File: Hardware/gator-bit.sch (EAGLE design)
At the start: 77 parts, among them J19 GATOR, J2 GATOR, J20 GATOR, J21 GATOR, J22 GATOR, J25 GATOR, J28 GATOR, J3 GATOR, J32 GATOR, J33 GATOR, J34 GATOR, J35 GATOR, J36 GATOR, J39 GATOR, J4 GATOR, J40 GATOR, U1 TPS63070, U2 micro:bit

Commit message: Updated Brd and Sch files
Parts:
- removed S2: (no value), SparkFun-Switches:SWITCH-SPDT-SMD-AYZ0202
- added C10, C11: 0.1uF, SparkFun-Capacitors:0.1UF-0603-25V-(+80/-20%)
- added C12, C13: 10uF, SparkFun-Capacitors:10UF-POLAR-EIA3216-16V-10%(TANT)
- added J1: GATOR, TAB:GATOR
- added S1: (no value), SparkFun-Switches:SWITCH-DPDT-SMD-AYZ0202
- added U3: 3.3V/150mA, SparkFun-IC-Power:V_REG_MIC52053.3V
- added U4: V_REG_MIC52053.0V, SparkFun-IC-Power:V_REG_MIC52053.0V
- C7: value 10uF -> 33UF; device SparkFun-Capacitors:10UF-0603-6.3V-20% -> SparkFun-Capacitors:33UF20%-6.3V-0805
- R3: value 274K -> 523k; device SparkFun-Resistors:274KOHMOHMS-0603-1/10W-1% -> SparkFun-Resistors:523KOHMOHMS-0603-1/10W-1%
- renumbered LOGO2 to GND
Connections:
- new net 3.0V: C10.1, C13.+, D11.C, D13.C, D15.C, D19.C, D21.C, D23.C, D25.C, U2.3.3V, U4.OUT
- new net 5V: C6.1, C9.1, R1.2, R3.2, S1.5, U1.VOUT, U3.EN, U3.IN, U4.EN, U4.IN
- new net VOUT5.0: J1.P$1, S1.6
- net 3.3V: now also C11.1, C12.+, S1.2, U3.OUT; no longer C6.1, C9.1, D11.C, D13.C, D15.C, D19.C, D21.C, D23.C, D25.C, R1.2, R3.2, S2.P, U1.VOUT, U2.3.3V
- net GND: now also C10.2, C11.2, C12.-, C13.-, U3.GND, U4.GND
- net P0: no longer R14.1
- net PD: now also R14.1
- net VOUT3.3: now also S1.3; no longer S2.S

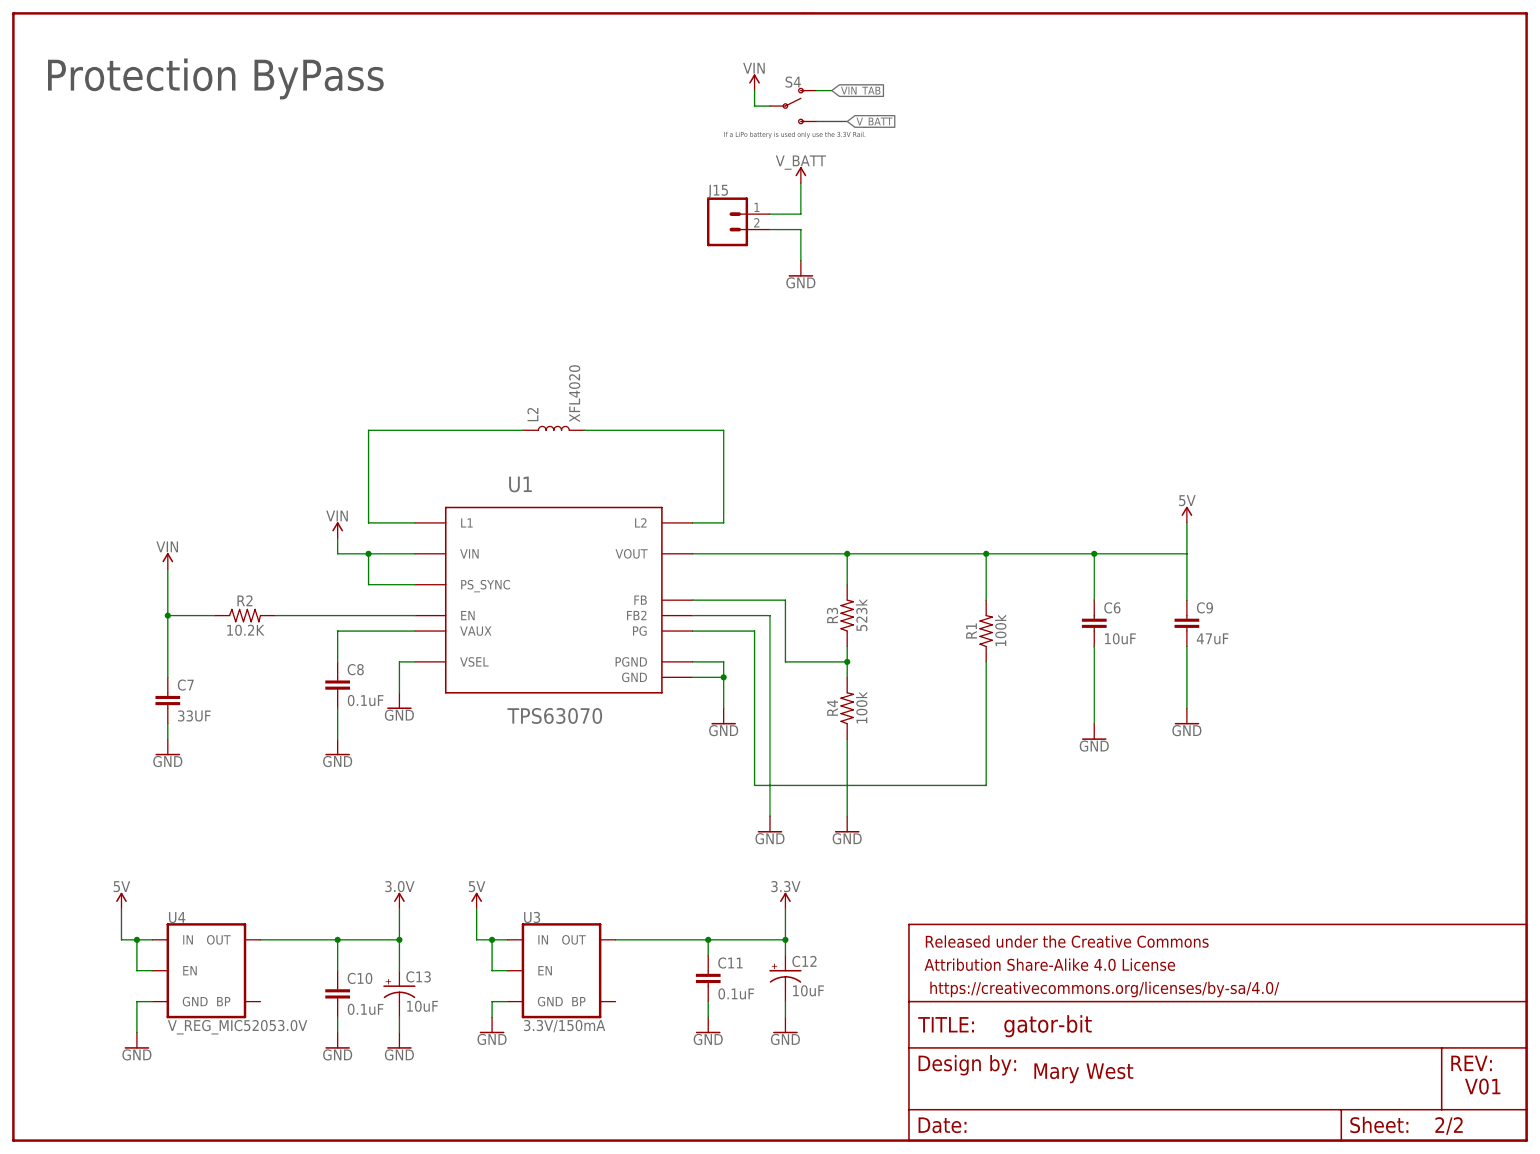
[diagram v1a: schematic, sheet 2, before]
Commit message: added SOT223 package for 3.3V regulated output
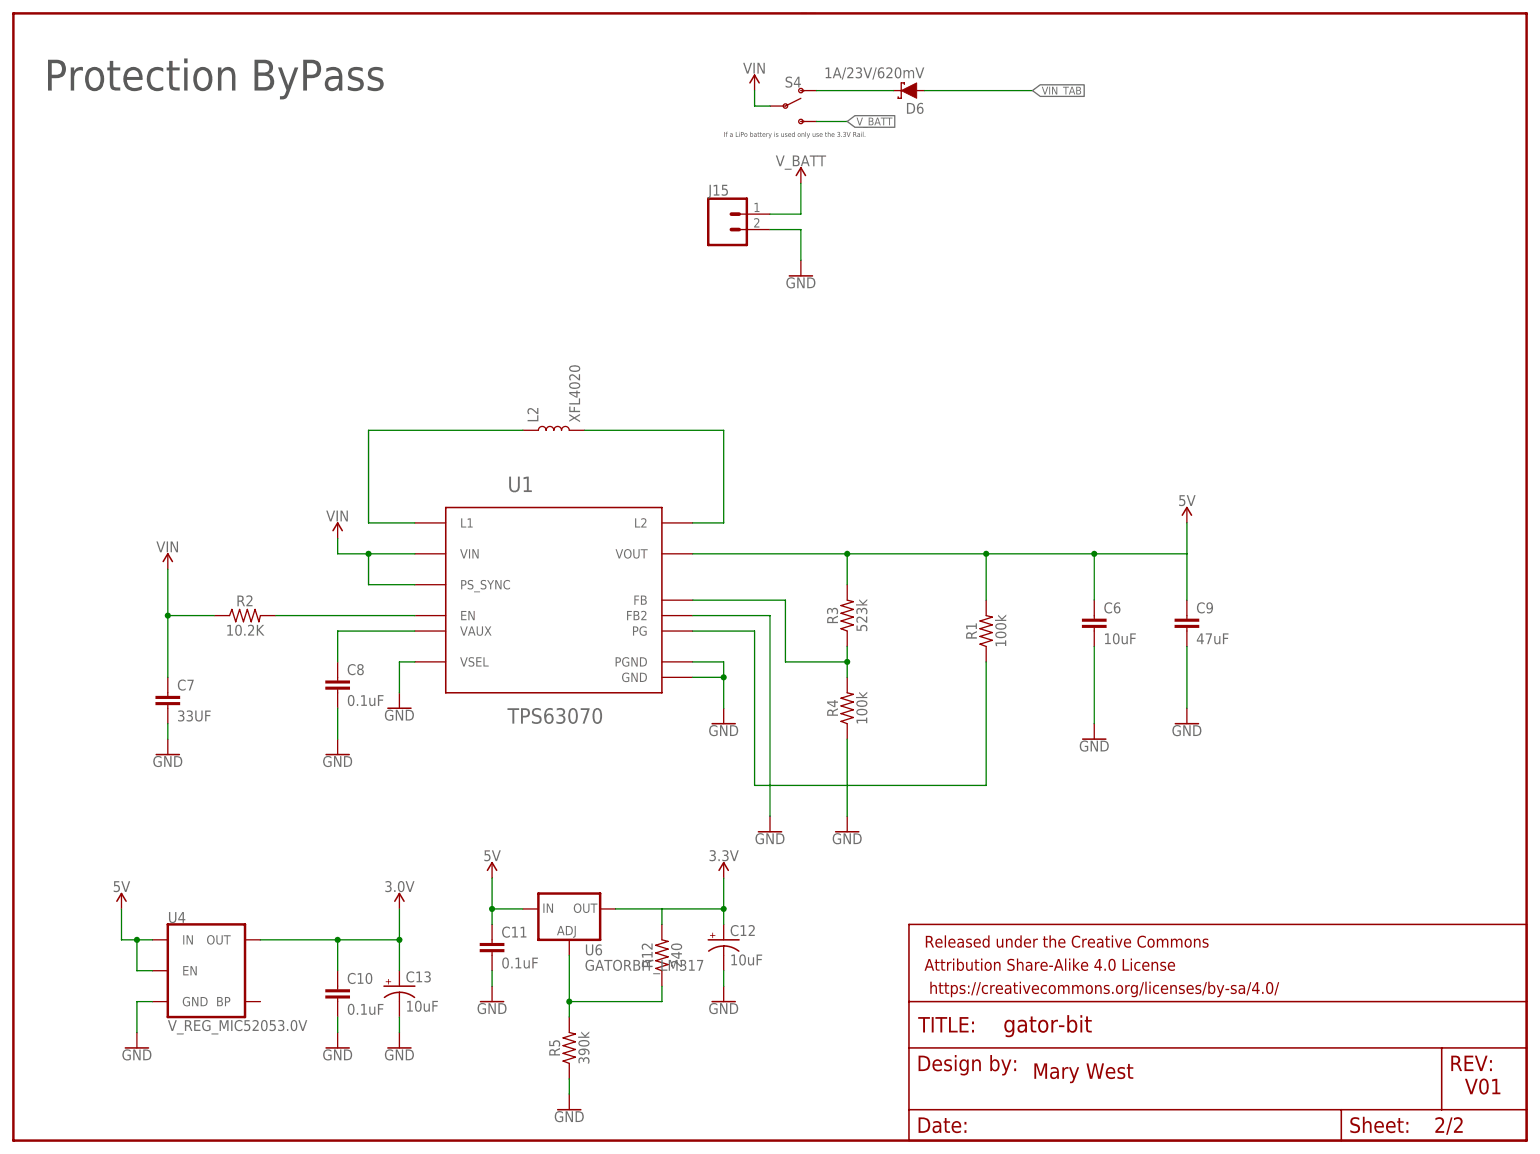
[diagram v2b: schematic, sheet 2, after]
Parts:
- removed U3: 3.3V/150mA, SparkFun-IC-Power:V_REG_MIC52053.3V
- added D6: 1A/23V/620mV, SparkFun-DiscreteSemi:DIODE-SCHOTTKY-BAT20J
- added FD3: FIDUCIAL1X2, SparkFun-Aesthetics:FIDUCIAL1X2
- added LOGO3: SFE_LOGO_NAME_FLAME.3_INCH, SparkFun-Aesthetics:SFE_LOGO_NAME_FLAME.3_INCH
- added R12: 240, SparkFun-Resistors:240OHM-0603-1/10W-1%
- added R5: 390k, SparkFun-Resistors:390KOHM-0603-1/10W-1%
- added U6: GATORBIT_LM317, SparkFun-IC-Power:GATORBIT_LM317
- renumbered GND to LOGO2
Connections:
- new net N$16: R12.1, R5.2, U6.ADJ
- new net N$9: D6.C, S4.O
- net 3.3V: now also R12.2, U6.OUT; no longer C11.1, U3.OUT
- net 5V: now also C11.1, U6.IN; no longer U3.EN, U3.IN
- net GND: now also R5.1; no longer U3.GND
- net VIN_TAB: now also D6.A; no longer S4.O
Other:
- moved on the sheet: C11, C12
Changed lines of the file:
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@@
 <part name="SUPPLY5" library="SparkFun-PowerSymbols" deviceset="3.3V" device=""/>
 <part name="SUPPLY9" library="SparkFun-PowerSymbols" deviceset="3.3V" device=""/>
-<part name="GND" library="SparkFun-Aesthetics" deviceset="OSHW-LOGO" device="L" value="OSHW-LOGOL"/>
 <part name="D11" library="SparkFun-DiscreteSemi" deviceset="DIODE-ZENER" device="-MM3Z3V3T1G" value="3.3V"/>
 <part name="SUPPLY7" library="SparkFun-PowerSymbols" deviceset="3.3V" device="" value="3.0V"/>
@@
 <part name="GND18" library="SparkFun-PowerSymbols" deviceset="GND" device=""/>
 <part name="GND20" library="SparkFun-PowerSymbols" deviceset="GND" device=""/>
-<part name="U3" library="SparkFun-IC-Power" deviceset="V_REG_MIC5205" device="3.3V" value="3.3V/150mA"/>
 <part name="U4" library="SparkFun-IC-Power" deviceset="V_REG_MIC5205" device="3.0V"/>
 <part name="SUPPLY20" library="SparkFun-PowerSymbols" deviceset="5V" device=""/>
@@
 <part name="SUPPLY26" library="SparkFun-PowerSymbols" deviceset="3.3V" device="" value="3.0V"/>
 <part name="SUPPLY27" library="SparkFun-PowerSymbols" deviceset="3.3V" device=""/>
+<part name="D6" library="SparkFun-DiscreteSemi" deviceset="DIODE-SCHOTTKY" device="-BAT20J" value="1A/23V/620mV"/>
+<part name="FD3" library="SparkFun-Aesthetics" deviceset="FIDUCIAL" device="1X2"/>
+<part name="LOGO2" library="SparkFun-Aesthetics" deviceset="OSHW-LOGO" device="L"/>
+<part name="LOGO3" library="SparkFun-Aesthetics" deviceset="SFE_LOGO_NAME_FLAME" device=".3_INCH"/>
+<part name="U6" library="SparkFun-IC-Power" deviceset="GATORBIT_LM317" device=""/>
+<part name="R5" library="SparkFun-Resistors" deviceset="390KOHM" device="-0603-1/10W-1%" value="390k"/>
+<part name="R12" library="SparkFun-Resistors" deviceset="240OHM" device="-0603-1/10W-1%" value="240"/>
 <part name="GND28" library="SparkFun-PowerSymbols" deviceset="GND" device=""/>
 </parts>
@@
 <instance part="SUPPLY5" gate="G$1" x="7.62" y="96.52"/>
 <instance part="SUPPLY9" gate="G$1" x="86.36" y="35.56"/>
-<instance part="GND" gate="G$1" x="167.64" y="45.72"/>
 <instance part="D11" gate="G$1" x="218.44" y="66.04" rot="R90"/>
 <instance part="SUPPLY7" gate="G$1" x="218.44" y="71.12"/>
@@
 <instance part="SUPPLY24" gate="G$1" x="203.2" y="127"/>
 <instance part="SUPPLY25" gate="G$1" x="226.06" y="127"/>
+<instance part="FD3" gate="G$1" x="238.76" y="33.02"/>
+<instance part="LOGO2" gate="G$1" x="167.64" y="45.72"/>
+<instance part="LOGO3" gate="G$1" x="193.04" y="33.02"/>
 </instances>
 <busses>
@@
 <instance part="GND18" gate="1" x="177.8" y="66.04"/>
 <instance part="GND20" gate="1" x="193.04" y="68.58"/>
-<instance part="U3" gate="U1" x="91.44" y="27.94"/>
 <instance part="U4" gate="U1" x="33.02" y="27.94"/>
 <instance part="SUPPLY20" gate="G$1" x="193.04" y="101.6"/>
 <instance part="SUPPLY21" gate="G$1" x="17.78" y="38.1"/>
-<instance part="SUPPLY22" gate="G$1" x="76.2" y="38.1"/>
+<instance part="SUPPLY22" gate="G$1" x="78.74" y="43.18"/>
 <instance part="C10" gate="G$1" x="53.34" y="22.86"/>
-<instance part="C11" gate="G$1" x="114.3" y="25.4"/>
-<instance part="C12" gate="G$1" x="127" y="27.94"/>
+<instance part="C11" gate="G$1" x="78.74" y="30.48"/>
+<instance part="C12" gate="G$1" x="116.84" y="33.02"/>
 <instance part="C13" gate="G$1" x="63.5" y="25.4"/>
 <instance part="GND21" gate="1" x="53.34" y="15.24"/>
 <instance part="GND23" gate="1" x="63.5" y="15.24"/>
-<instance part="GND24" gate="1" x="114.3" y="17.78"/>
-<instance part="GND25" gate="1" x="127" y="17.78"/>
+<instance part="GND24" gate="1" x="78.74" y="22.86"/>
+<instance part="GND25" gate="1" x="116.84" y="22.86"/>
 <instance part="GND27" gate="1" x="20.32" y="15.24"/>
 <instance part="SUPPLY26" gate="G$1" x="63.5" y="38.1"/>
-<instance part="SUPPLY27" gate="G$1" x="127" y="38.1"/>
-<instance part="GND28" gate="1" x="78.74" y="17.78"/>
+<instance part="SUPPLY27" gate="G$1" x="116.84" y="43.18"/>
+<instance part="D6" gate="G$1" x="147.32" y="172.72" rot="R180"/>
+<instance part="U6" gate="G$1" x="91.44" y="38.1"/>
+<instance part="R5" gate="G$1" x="91.44" y="15.24" rot="R90"/>
+<instance part="R12" gate="G$1" x="106.68" y="30.48" rot="R90"/>
+<instance part="GND28" gate="1" x="91.44" y="5.08"/>
 </instances>
 <busses>
@@
 <pinref part="C11" gate="G$1" pin="2"/>
 <pinref part="GND24" gate="1" pin="GND"/>
-<wire x1="114.3" y1="22.86" x2="114.3" y2="20.32" width="0.1524" layer="91"/>
+<wire x1="78.74" y1="27.94" x2="78.74" y2="25.4" width="0.1524" layer="91"/>
 </segment>
 <segment>
 <pinref part="C12" gate="G$1" pin="-"/>
 <pinref part="GND25" gate="1" pin="GND"/>
-<wire x1="127" y1="22.86" x2="127" y2="20.32" width="0.1524" layer="91"/>
-</segment>
-<segment>
-<pinref part="U3" gate="U1" pin="GND"/>
-<wire x1="81.28" y1="22.86" x2="78.74" y2="22.86" width="0.1524" layer="91"/>
+<wire x1="116.84" y1="27.94" x2="116.84" y2="25.4" width="0.1524" layer="91"/>
+</segment>
+<segment>
+<pinref part="R5" gate="G$1" pin="1"/>
+<wire x1="91.44" y1="10.16" x2="91.44" y2="7.62" width="0.1524" layer="91"/>
 <pinref part="GND28" gate="1" pin="GND"/>
-<wire x1="78.74" y1="22.86" x2="78.74" y2="20.32" width="0.1524" layer="91"/>
 </segment>
 </net>
@@
 <net name="VIN_TAB" class="0">
 <segment>
-<pinref part="S4" gate="1" pin="O"/>
-<wire x1="132.08" y1="172.72" x2="134.62" y2="172.72" width="0.1524" layer="91"/>
-<label x="134.62" y="172.72" size="1.27" layer="95" xref="yes"/>
+<label x="167.64" y="172.72" size="1.27" layer="95" xref="yes"/>
+<pinref part="D6" gate="G$1" pin="A"/>
+<wire x1="149.86" y1="172.72" x2="167.64" y2="172.72" width="0.1524" layer="91"/>
 </segment>
 </net>
@@
 </segment>
 <segment>
-<pinref part="U3" gate="U1" pin="IN"/>
-<wire x1="81.28" y1="33.02" x2="78.74" y2="33.02" width="0.1524" layer="91"/>
-<wire x1="78.74" y1="33.02" x2="76.2" y2="33.02" width="0.1524" layer="91"/>
-<wire x1="76.2" y1="33.02" x2="76.2" y2="38.1" width="0.1524" layer="91"/>
+<wire x1="83.82" y1="38.1" x2="78.74" y2="38.1" width="0.1524" layer="91"/>
+<wire x1="78.74" y1="38.1" x2="78.74" y2="43.18" width="0.1524" layer="91"/>
 <pinref part="SUPPLY22" gate="G$1" pin="5V"/>
-<pinref part="U3" gate="U1" pin="EN"/>
-<wire x1="81.28" y1="27.94" x2="78.74" y2="27.94" width="0.1524" layer="91"/>
-<wire x1="78.74" y1="27.94" x2="78.74" y2="33.02" width="0.1524" layer="91"/>
-<junction x="78.74" y="33.02"/>
+<pinref part="U6" gate="G$1" pin="IN"/>
+<pinref part="C11" gate="G$1" pin="1"/>
+<wire x1="78.74" y1="35.56" x2="78.74" y2="38.1" width="0.1524" layer="91"/>
+<junction x="78.74" y="38.1"/>
 </segment>
 </net>
@@
 <segment>
 <pinref part="SUPPLY27" gate="G$1" pin="3.3V"/>
-<wire x1="127" y1="38.1" x2="127" y2="33.02" width="0.1524" layer="91"/>
-</segment>
-<segment>
-<pinref part="U3" gate="U1" pin="OUT"/>
-<wire x1="99.06" y1="33.02" x2="114.3" y2="33.02" width="0.1524" layer="91"/>
+<wire x1="116.84" y1="43.18" x2="116.84" y2="38.1" width="0.1524" layer="91"/>
+</segment>
+<segment>
+<wire x1="99.06" y1="38.1" x2="106.68" y2="38.1" width="0.1524" layer="91"/>
 <pinref part="C12" gate="G$1" pin="+"/>
-<wire x1="114.3" y1="33.02" x2="127" y2="33.02" width="0.1524" layer="91"/>
-<wire x1="127" y1="33.02" x2="127" y2="30.48" width="0.1524" layer="91"/>
-<pinref part="C11" gate="G$1" pin="1"/>
-<wire x1="114.3" y1="30.48" x2="114.3" y2="33.02" width="0.1524" layer="91"/>
-<junction x="114.3" y="33.02"/>
-<junction x="127" y="33.02"/>
-</segment>
-</net>
+<wire x1="106.68" y1="38.1" x2="116.84" y2="38.1" width="0.1524" layer="91"/>
+<wire x1="116.84" y1="38.1" x2="116.84" y2="35.56" width="0.1524" layer="91"/>
+<junction x="116.84" y="38.1"/>
+<pinref part="U6" gate="G$1" pin="OUT"/>
+<pinref part="R12" gate="G$1" pin="2"/>
+<wire x1="106.68" y1="35.56" x2="106.68" y2="38.1" width="0.1524" layer="91"/>
+</segment>
+</net>
+<net name="N$9" class="0">
+<segment>
+<pinref part="D6" gate="G$1" pin="C"/>
+<pinref part="S4" gate="1" pin="O"/>
+<wire x1="132.08" y1="172.72" x2="144.78" y2="172.72" width="0.1524" layer="91"/>
+</segment>
+</net>
+<net name="N$16" class="0">
+<segment>
+<pinref part="U6" gate="G$1" pin="ADJ"/>
+<pinref part="R5" gate="G$1" pin="2"/>
+<wire x1="91.44" y1="30.48" x2="91.44" y2="22.86" width="0.1524" layer="91"/>
+<pinref part="R12" gate="G$1" pin="1"/>
+<wire x1="91.44" y1="22.86" x2="91.44" y2="20.32" width="0.1524" layer="91"/>
+<wire x1="106.68" y1="25.4" x2="106.68" y2="22.86" width="0.1524" layer="91"/>
+<wire x1="106.68" y1="22.86" x2="91.44" y2="22.86" width="0.1524" layer="91"/>
+<junction x="91.44" y="22.86"/>
+</segment>
+</net>
